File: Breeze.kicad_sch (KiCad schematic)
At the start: 102 parts

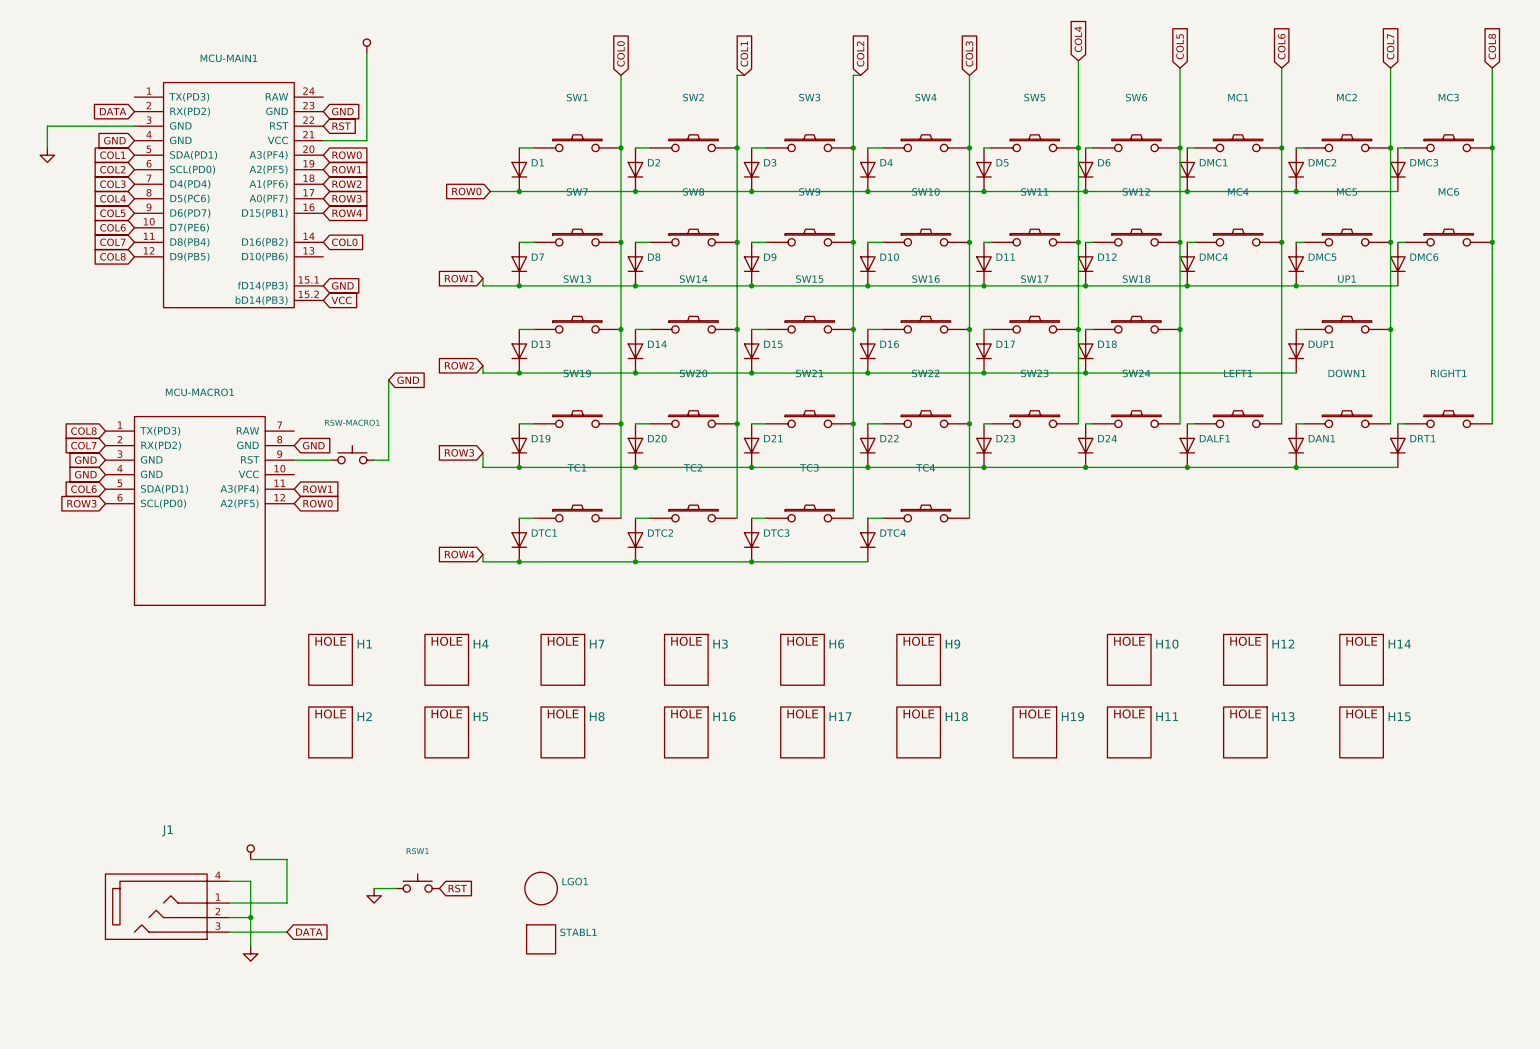
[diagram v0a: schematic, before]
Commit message: Update KiCAD format
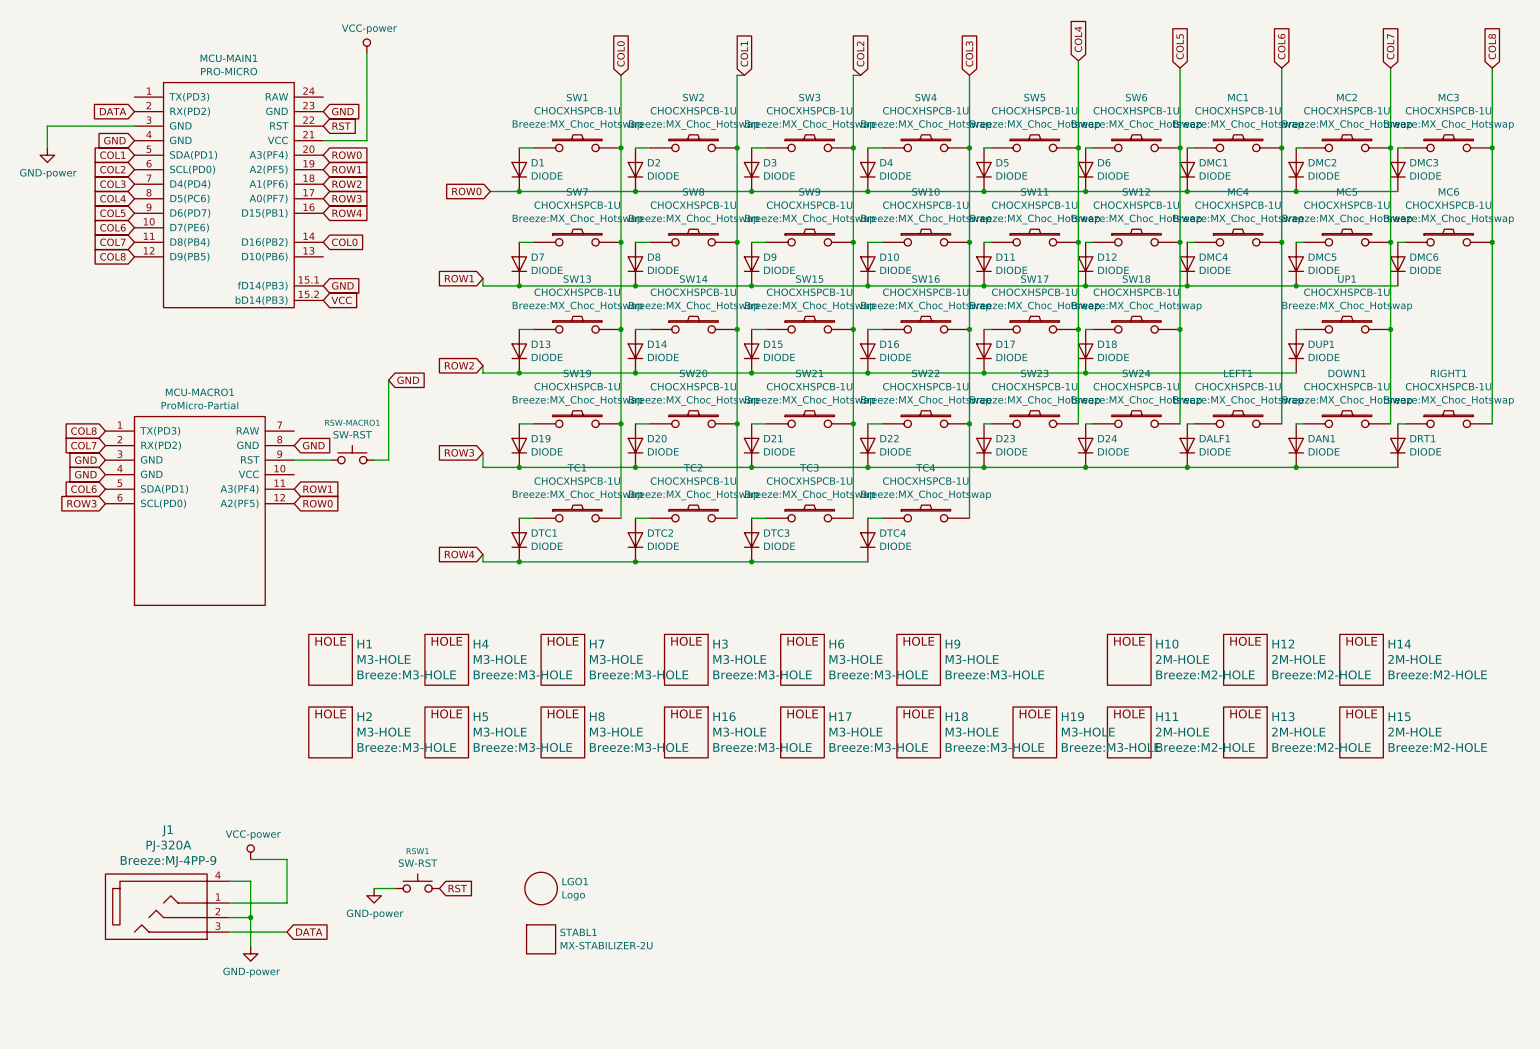
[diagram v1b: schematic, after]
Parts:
- D1, D10, D11, D12, D13, D14, D15, D16, D17, D18, D19, D2, D20, D21, D22, D23, D24, D3, D4, D5, D6, D7, D8, D9, DALF1, DAN1, DMC1, DMC2, DMC3, DMC4, DMC5, DMC6, DRT1, DTC1, DTC2, DTC3, DTC4, DUP1: value (none) -> DIODE; footprint (none) -> Breeze:SOD-123FL
- DOWN1, LEFT1, MC1, MC2, MC3, MC4, MC5, MC6, RIGHT1, SW1, SW10, SW11, SW12, SW13, SW14, SW15, SW16, SW17, SW18, SW19, SW2, SW20, SW21, SW22, SW23, SW24, SW3, SW4, SW5, SW6, SW7, SW8, SW9, TC1, TC2, TC3, TC4, UP1: value (none) -> CHOCXHSPCB-1U; footprint (none) -> Breeze:MX_Choc_Hotswap
- H1, H16, H17, H18, H19, H2, H3, H4, H5, H6, H7, H8, H9: value (none) -> M3-HOLE; footprint (none) -> Breeze:M3-HOLE
- H10, H11, H12, H13, H14, H15: value (none) -> 2M-HOLE; footprint (none) -> Breeze:M2-HOLE
- J1: value (none) -> PJ-320A; footprint (none) -> Breeze:MJ-4PP-9
- LGO1: value (none) -> Logo; footprint (none) -> Breeze:logo
- MCU-MACRO1: value (none) -> ProMicro-Partial; footprint (none) -> Breeze:PROMICRO-PARTIAL2
- MCU-MAIN1: value (none) -> PRO-MICRO; footprint (none) -> Breeze:ProMicro
- RSW-MACRO1, RSW1: value (none) -> SW-RST; footprint (none) -> Breeze:TACT_SWITCH_TVBP06
- STABL1: value (none) -> MX-STABILIZER-2U; footprint (none) -> Breeze:Stabilizer_MX_2u

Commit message: Switch interconnect TRRS to USB-C, change to SMD reset button (rerouting of traces not done)
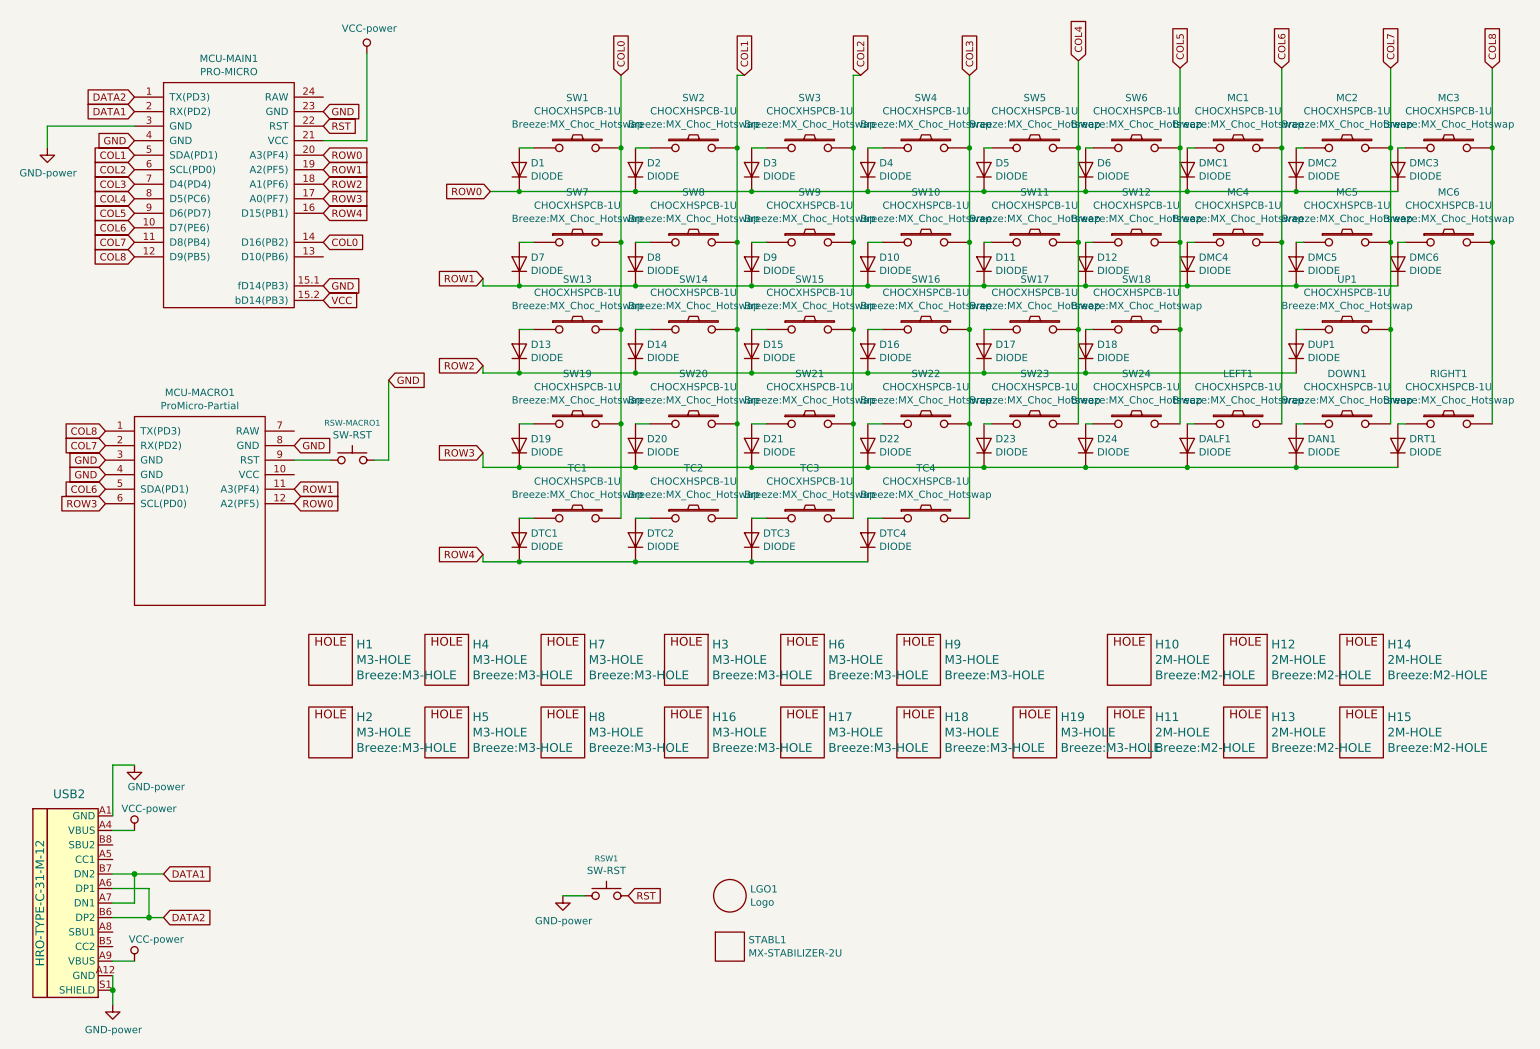
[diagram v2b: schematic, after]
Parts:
- removed J1: PJ-320A, Breeze:MJ-4PP-9, symbol Breeze-rescue:MJ-4PP-9-Lily58-cache-Merkaba_Rev0-rescue-Breeze-rescue
- added USB2: HRO-TYPE-C-31-M-12, Connector_USB:USB_C_Receptacle_HRO_TYPE-C-31-M-12, symbol keebio:HRO-TYPE-C-31-M-12
- RSW1: footprint Breeze:TACT_SWITCH_TVBP06 -> Button_Switch_SMD:SW_SPST_TL3342
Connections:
- net GND: now also USB2.A1 (GND), USB2.A12 (GND), USB2.S1 (SHIELD)
- net VCC: now also USB2.A4 (VBUS), USB2.A9 (VBUS)
- net DATA2: now reaches MCU-MAIN1.1 (TX(PD3))
- net DATA2: now also USB2.A6 (DP1), USB2.B6 (DP2)
- net DATA renamed DATA1
- net DATA1: now also USB2.A7 (DN1), USB2.B7 (DN2)
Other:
- moved on the sheet: LGO1, RSW1, STABL1
